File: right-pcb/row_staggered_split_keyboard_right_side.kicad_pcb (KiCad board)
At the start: 2 copper layers, 165 x 132 mm, 177 parts, among them J1 Conn_01x02, SW1 SW_SPST, SW10 SW_SPST, SW11 SW_SPST, SW12 SW_SPST, SW13 SW_SPST, SW14 SW_SPST, SW15 SW_SPST, SW16 SW_SPST, SW17 SW_SPST, SW18 SW_SPST, SW19 SW_SPST, SW2 SW_SPST, SW20 SW_SPST, SW21 SW_SPST, SW22 SW_SPST, SW23 SW_SPST, SW24 SW_SPST, SW25 SW_SPST, SW26 SW_SPST, SW27 SW_SPST, SW28 SW_SPST, SW29 SW_SPST, SW3 SW_SPST, SW30 SW_SPST, SW31 SW_SPST, SW32 SW_SPST, SW33 SW_SPST, SW34 SW_SPST, SW35 SW_SPST, SW36 SW_SPST, SW37 SW_SPST, SW38 SW_SPST, SW39 SW_SPST, SW4 SW_SPST, SW40 SW_SPST, SW41 SW_SPST, SW5 SW_SPST, SW6 SW_SPST, SW7 SW_SPST, SW8 SW_SPST, SW9 SW_SPST, U1 SN74LVC1T45DBV

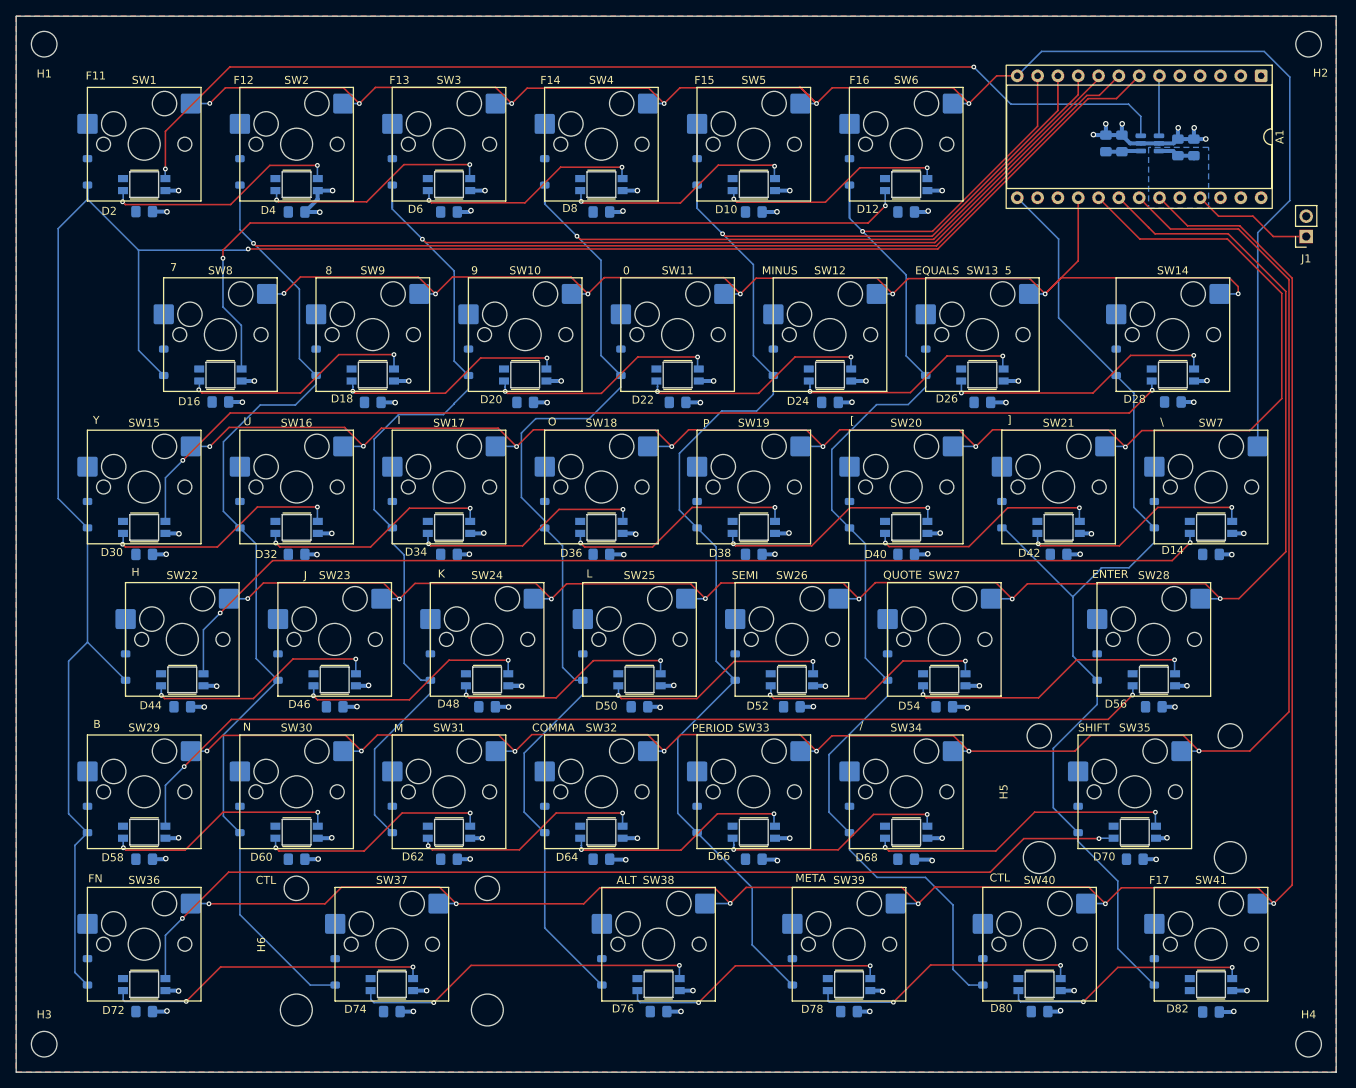
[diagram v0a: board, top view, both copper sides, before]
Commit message: reworking LED data lines to eliminate ground plane disconnections
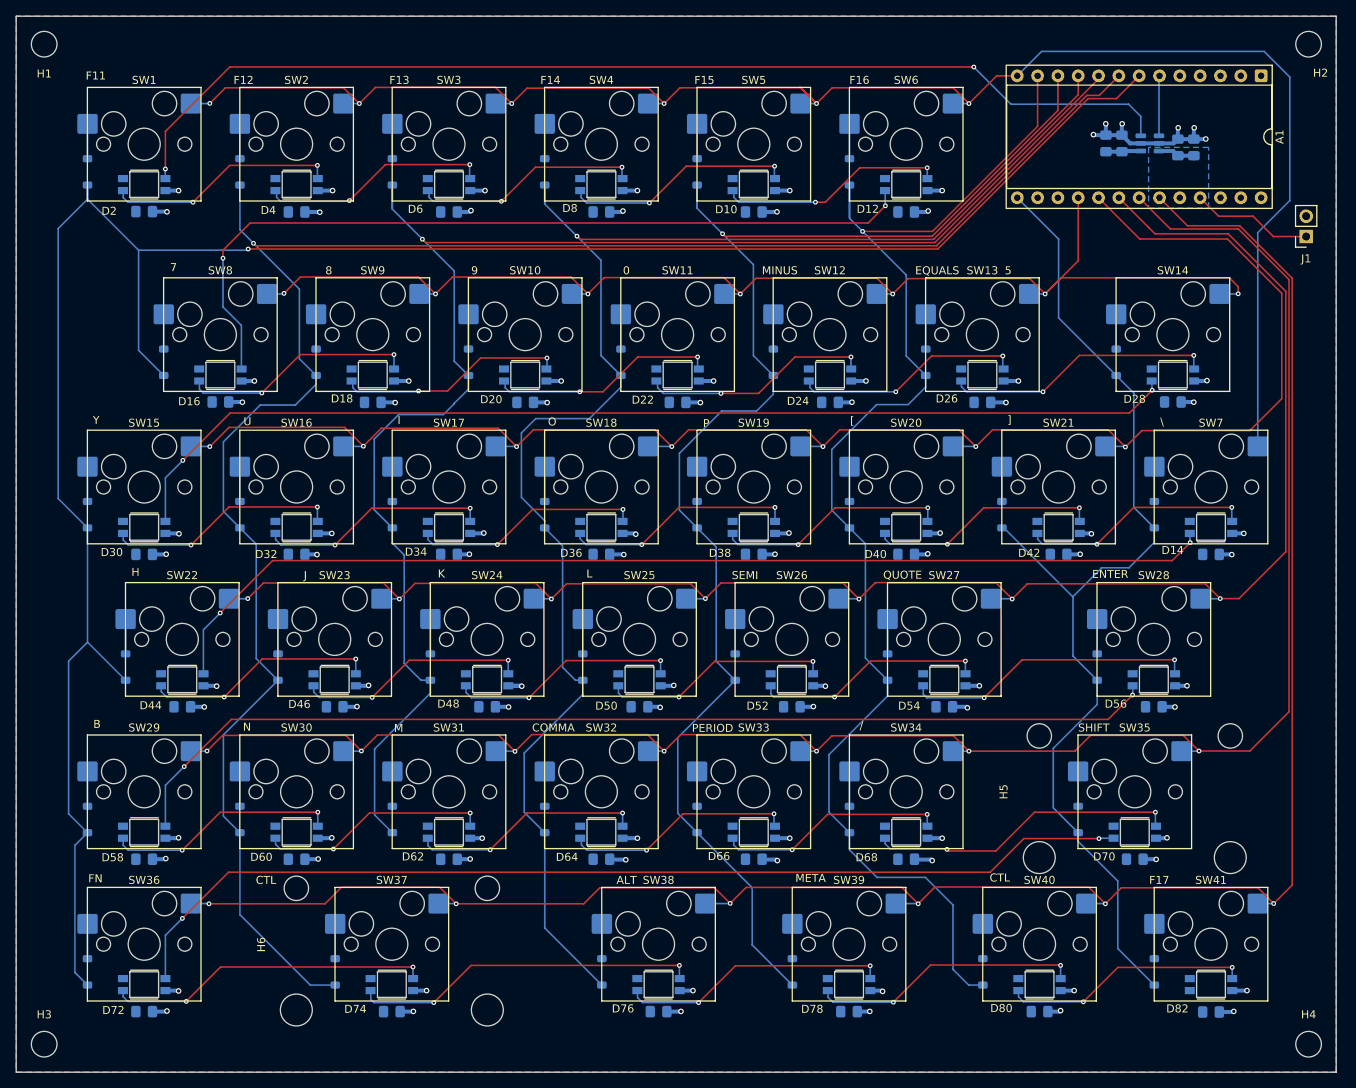
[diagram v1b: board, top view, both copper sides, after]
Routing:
- net GND: track 169.5 -> 166.2 mm
- net /R1C0/DOUT: track 29.6 -> 28.9 mm
- net /R3C0/DOUT: track 29.7 -> 29.1 mm
- net /R1C3/DOUT: track 29.2 -> 28.6 mm
- net /R2C5/DOUT: track 34.2 -> 33.6 mm
- net /R4C1/DOUT: track 29.6 -> 29.0 mm
- net /R3C3/DOUT: track 29.5 -> 28.9 mm
- net /R3C5/DOUT: track 29.3 -> 28.8 mm

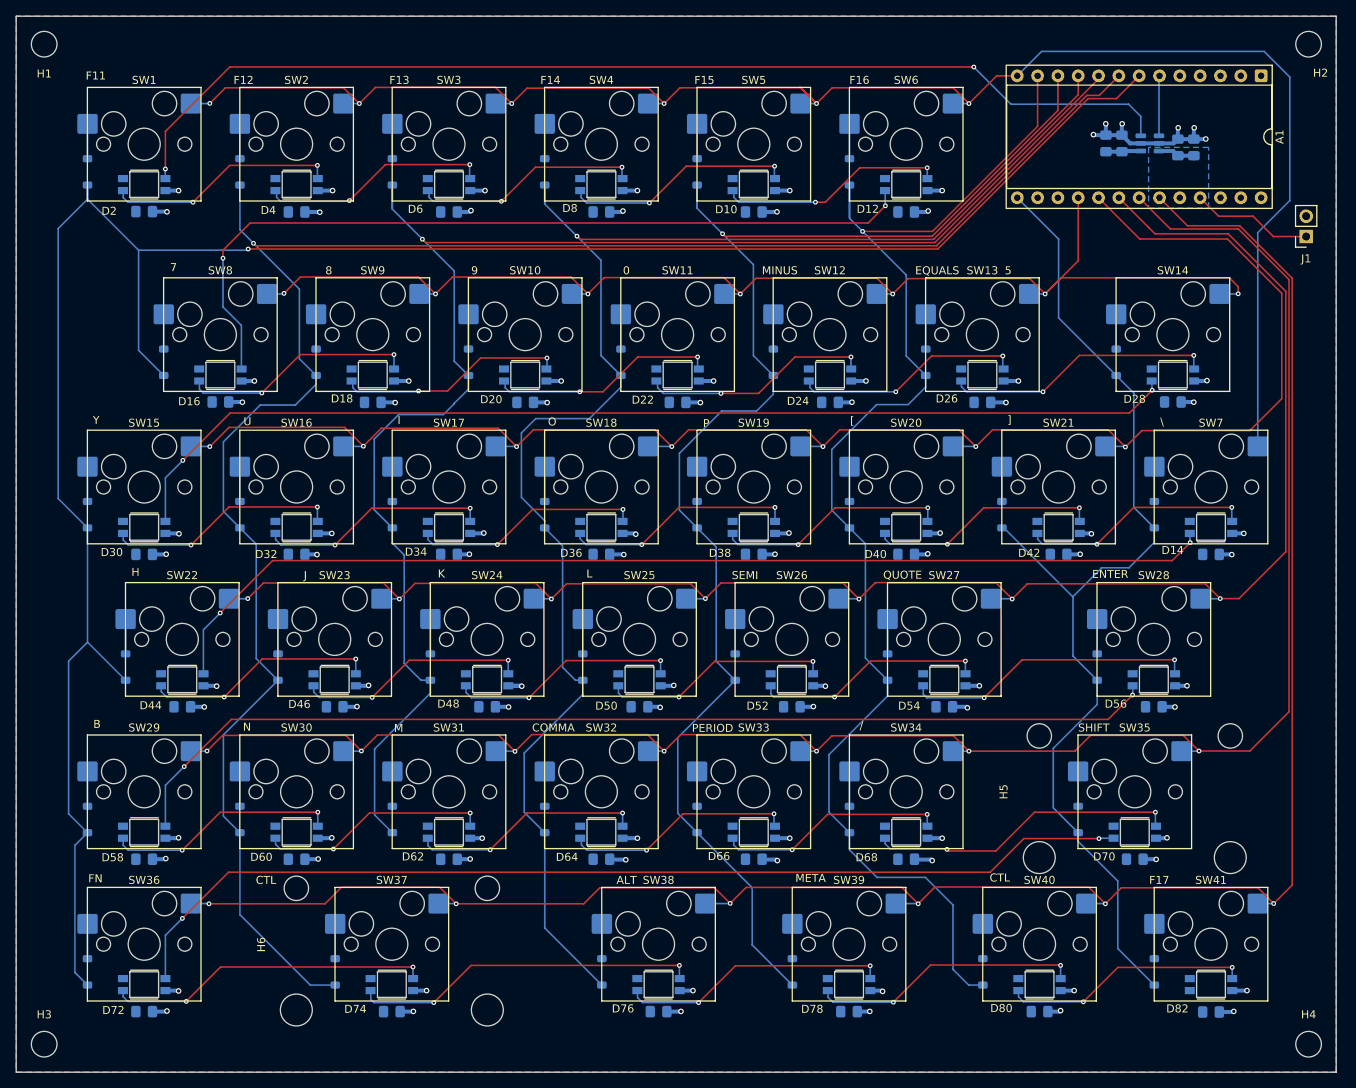
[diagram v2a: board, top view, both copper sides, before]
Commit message: Silkscreen cleanup and trace cleanup in prep for PCB review posting
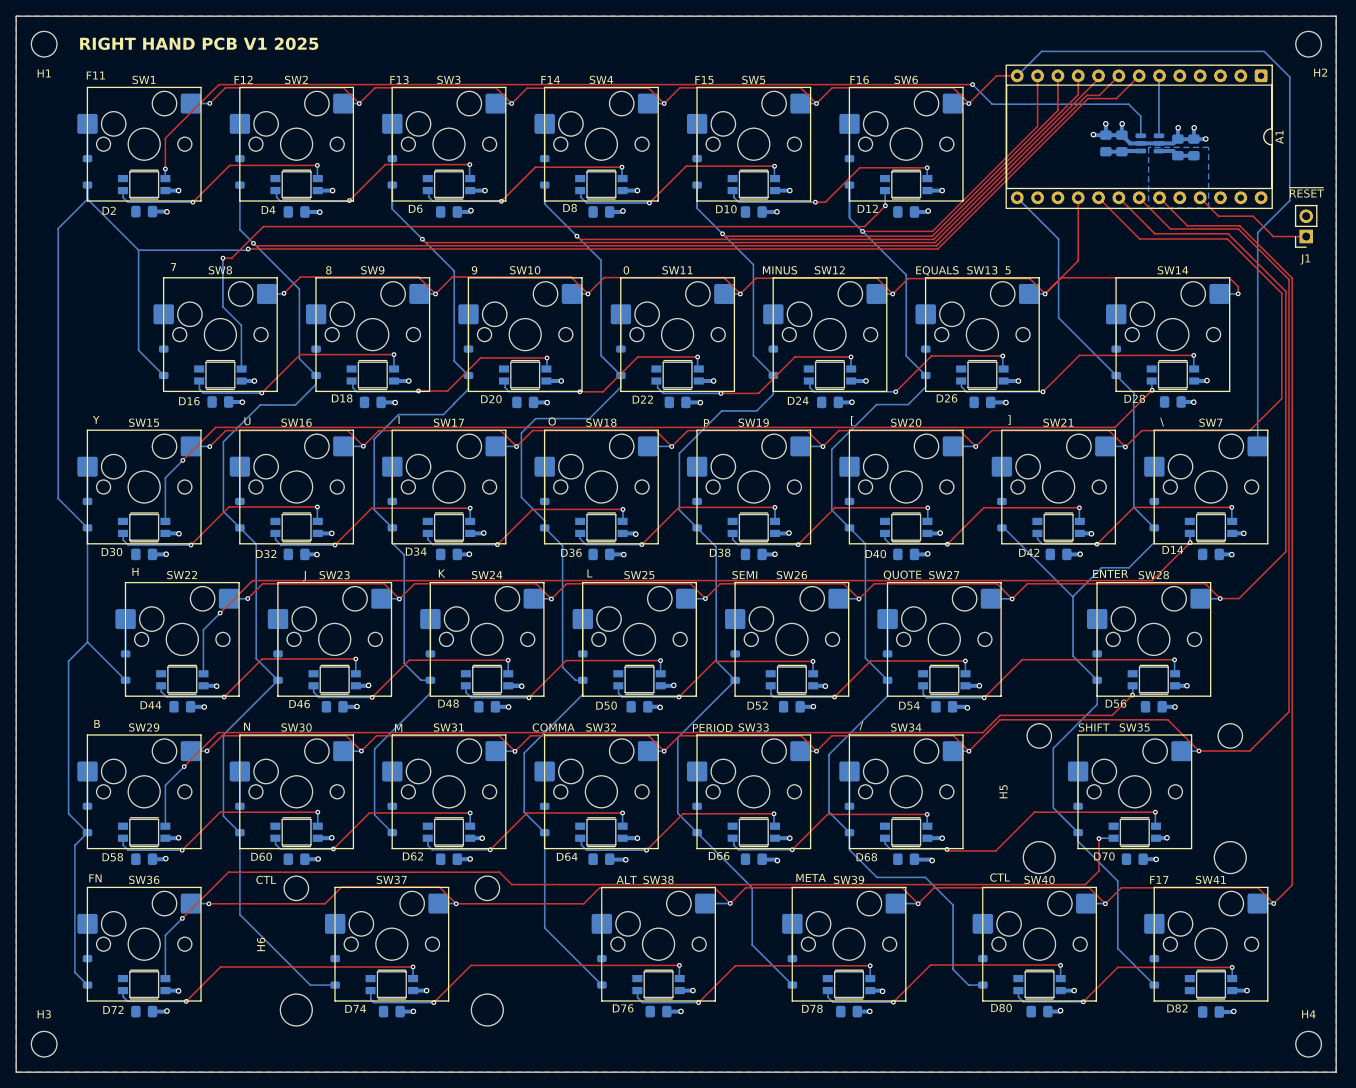
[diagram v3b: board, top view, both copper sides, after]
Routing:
- net /R5C6/DOUT: track 129.0 -> 132.6 mm
- net /ROW1: track 210.4 -> 207.3 mm
- net /LED_DATA: track 136.2 -> 133.8 mm
- net /ROW5: track 239.1 -> 240.4 mm
- net /ROW3: track 207.1 -> 206.1 mm
- net /R1C5/DOUT: track 102.8 -> 102.2 mm
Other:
- board text added: "RIGHT HAND PCB V1 2025"
- board text added: "~{RESET}"
